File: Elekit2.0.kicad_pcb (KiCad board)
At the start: 2 copper layers, 25 parts, among them J1 USB_C_Receptacle_USB2.0, Q1 AO3401A, SW1 SW_Push, SW2 SW_Push, U1 ESP32-C3-WROOM-02-H4, U2 XC6206P332MR, U3 SRV05-4-P-T7

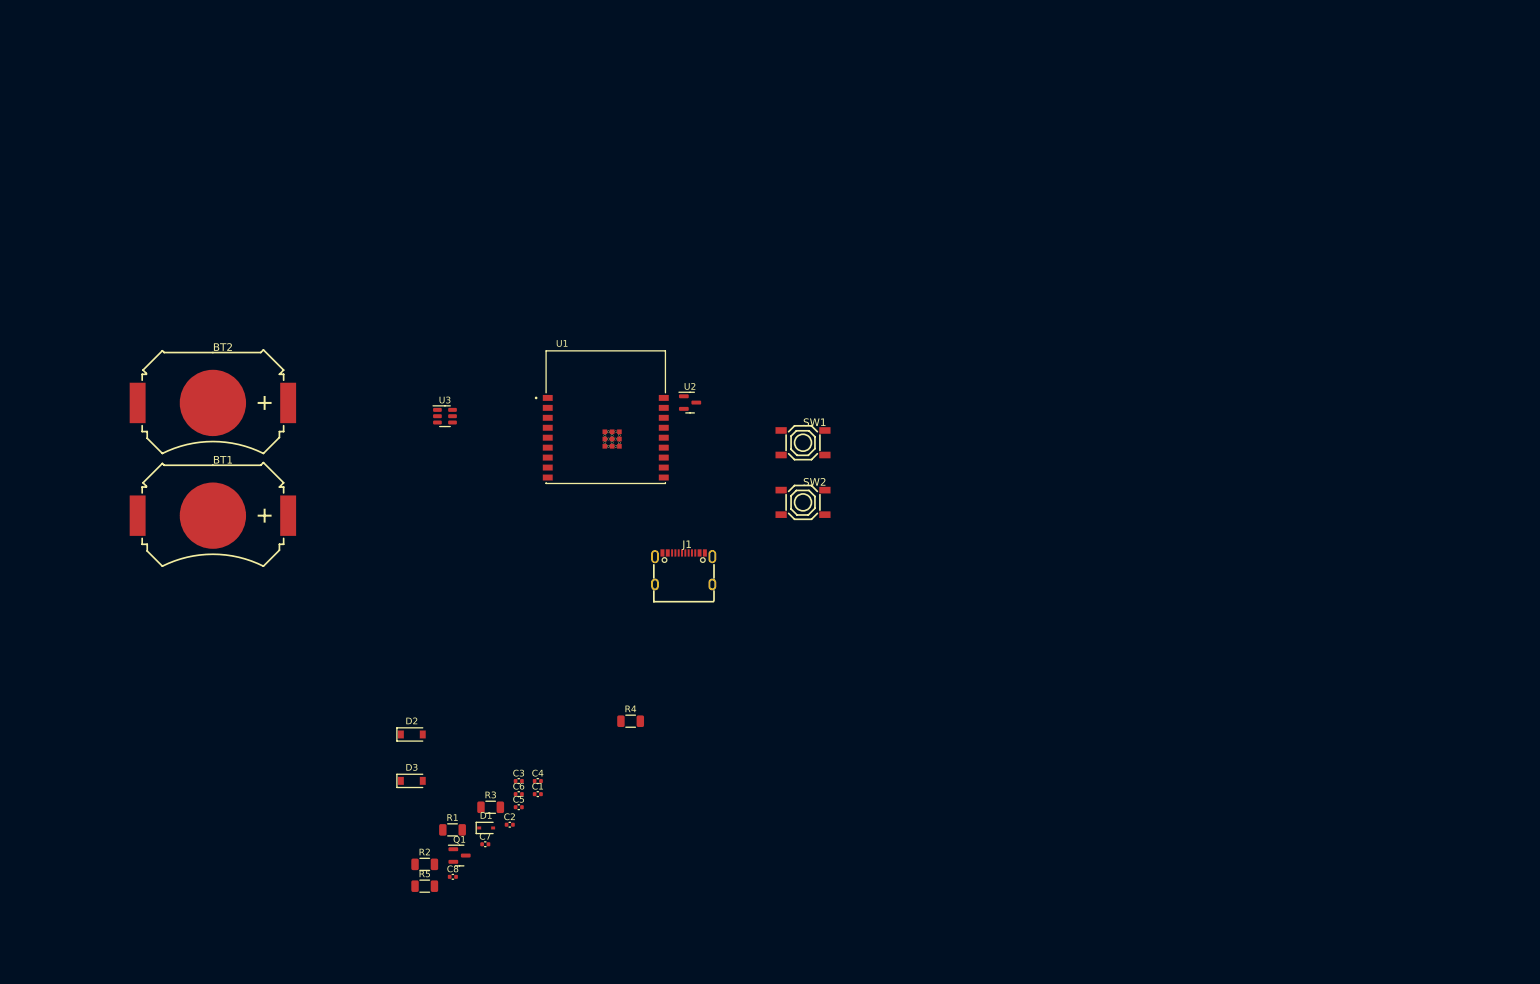
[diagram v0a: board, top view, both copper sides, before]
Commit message: Add libraries for used JLCPCB parts. Replace used parts with JLCPCB parts. Start adding LCD support using a shift register
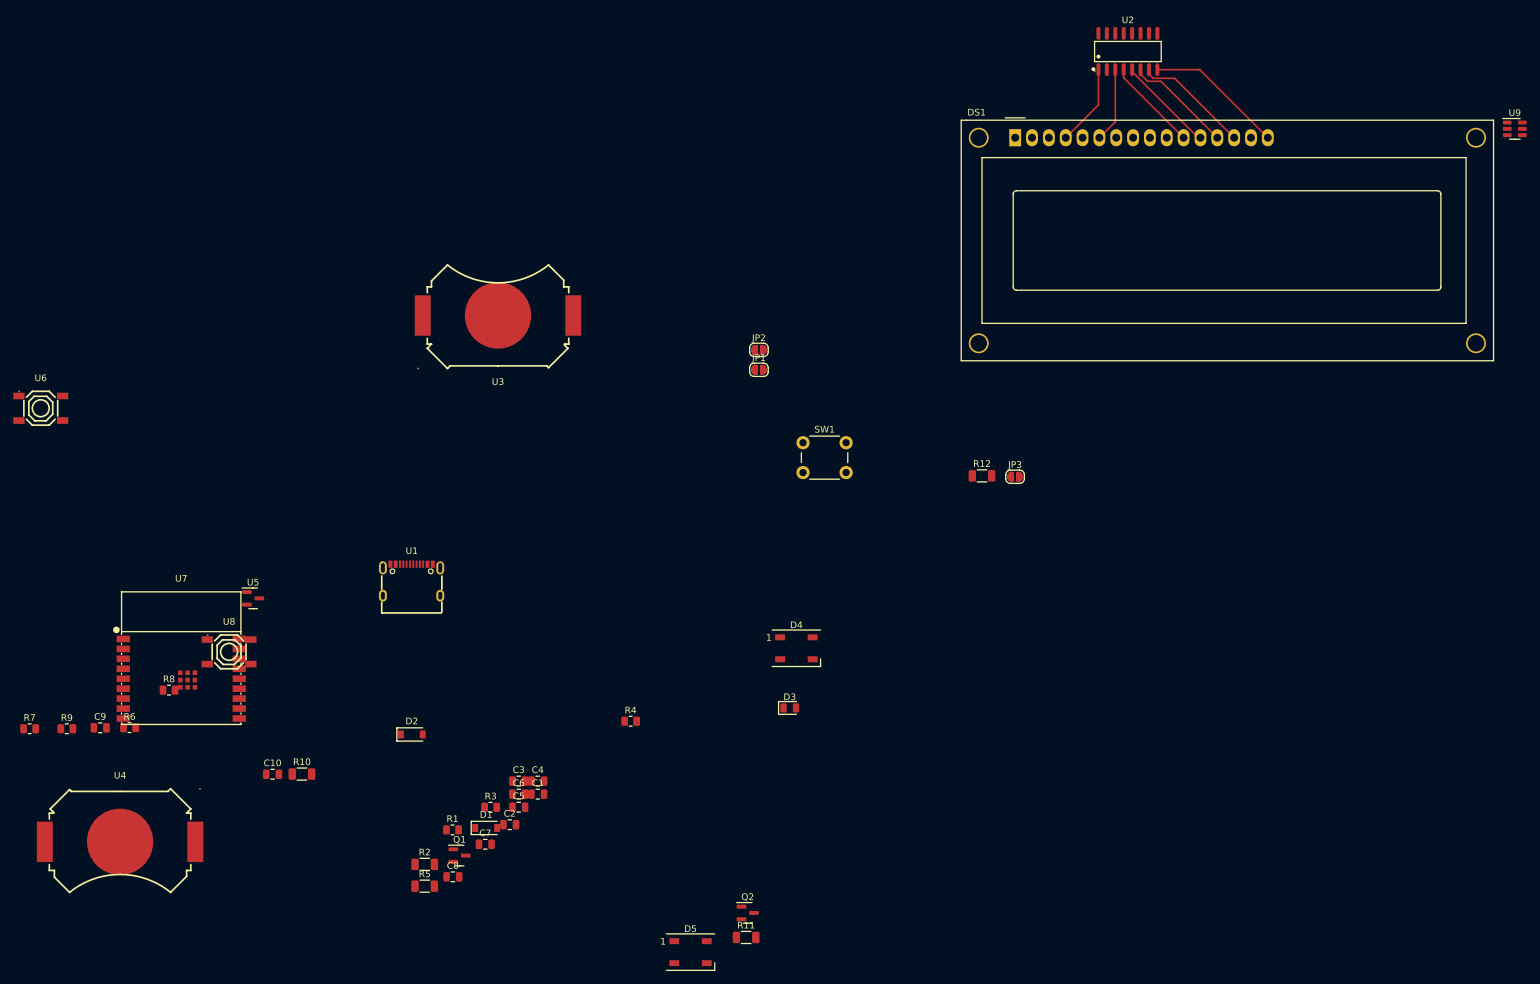
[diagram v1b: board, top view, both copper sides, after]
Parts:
- removed BT1, BT2: Battery_Cell, Footprint Libaries:BAT-SMD_MY-2032-12
- removed J1: USB_C_Receptacle_USB2.0, Footprint Libaries:USB-C-SMD_TYPE-C-6PIN-2MD-073
- removed SW2: SW_Push, Footprint Libaries:SW-SMD_4P-L5.1-W5.1-P3.70-LS6.5-TL-2
- added C10: 0.1u, Capacitor_SMD:C_0805_2012Metric, F.Cu at (87.0, 134.0)
- added C9: 0.1u, Capacitor_SMD:C_0805_2012Metric, F.Cu at (61.0, 127.0)
- added D4: WS2812B, LED_SMD:LED_WS2812B_PLCC4_5.0x5.0mm_P3.2mm, F.Cu at (166.0, 115.0)
- added D5: WS2812B, LED_SMD:LED_WS2812B_PLCC4_5.0x5.0mm_P3.2mm, F.Cu at (150.0, 160.8)
- added DS1: WC1602A, Display:WC1602A, F.Cu at (199.0, 38.0)
- added JP1: SolderJumper_2_Open, Jumper:SolderJumper-2_P1.3mm_Open_RoundedPad1.0x1.5mm, F.Cu at (160.3, 73.0)
- added JP2: SolderJumper_2_Open, Jumper:SolderJumper-2_P1.3mm_Open_RoundedPad1.0x1.5mm, F.Cu at (160.3, 70.0)
- added JP3: SolderJumper_2_Open, Jumper:SolderJumper-2_P1.3mm_Open_RoundedPad1.0x1.5mm, F.Cu at (199.0, 89.1)
- added Q2: 2N7002, Package_TO_SOT_SMD:SOT-23, F.Cu at (158.7, 154.9)
- added R10: 10k, Resistor_SMD:R_1206_3216Metric, F.Cu at (91.4, 134.0)
- added R11: 10k, Resistor_SMD:R_1206_3216Metric, F.Cu at (158.4, 158.6)
- added R12: 10k, Resistor_SMD:R_1206_3216Metric, F.Cu at (194.0, 89.0)
- added R6: 1k, Resistor_SMD:R_0805_2012Metric, F.Cu at (65.4, 127.0)
- added R7: 1k, Resistor_SMD:R_0805_2012Metric, F.Cu at (50.4, 127.1)
- added R8: 1k, Resistor_SMD:R_0805_2012Metric, F.Cu at (71.4, 121.3)
- added R9: 5.1k, Resistor_SMD:R_0805_2012Metric, F.Cu at (56.0, 127.1)
- added U4: MY-2032-12, 0_JLCPCB_Footprints:BAT-SMD_MY-2032-12, F.Cu at (64.0, 144.0)
- added U5: XC6206P332MR, Package_TO_SOT_SMD:SOT-23, F.Cu at (84.1, 107.5)
- added U6: TS-1187A-B-A-B, 0_JLCPCB_Footprints:SW-SMD_4P-L5.1-W5.1-P3.70-LS6.5-TL-2, F.Cu at (52.0, 78.8)
- added U7: ESP32-C3-WROOM-02-N4(4MB), 0_JLCPCB_Footprints:BULETM-SMD_ESPRESSIF_ESP32-C3-WROOM-02-N4-4MB, F.Cu at (73.2, 116.5)
- added U8: TS-1187A-B-A-B, 0_JLCPCB_Footprints:SW-SMD_4P-L5.1-W5.1-P3.70-LS6.5-TL-2, F.Cu at (80.4, 115.5)
- added U9: SRV05-4-P-T7, Package_TO_SOT_SMD:SOT-23-6, F.Cu at (274.4, 36.7)
- C1, C2: value 1u -> 0.1u; footprint Capacitor_SMD:C_0402_1005Metric -> Capacitor_SMD:C_0805_2012Metric
- C3: value 0.1u -> 4.7n; footprint Capacitor_SMD:C_0402_1005Metric -> Capacitor_SMD:C_0805_2012Metric
- C4, C6: value 0.1u -> 1u; footprint Capacitor_SMD:C_0402_1005Metric -> Capacitor_SMD:C_0805_2012Metric
- C5: value 10u -> 1u; footprint Capacitor_SMD:C_0402_1005Metric -> Capacitor_SMD:C_0805_2012Metric
- C7: footprint Capacitor_SMD:C_0402_1005Metric -> Capacitor_SMD:C_0805_2012Metric
- C8: value 0.1u -> 10u; footprint Capacitor_SMD:C_0402_1005Metric -> Capacitor_SMD:C_0805_2012Metric
- D1: value 1N5819WS -> B5819W; footprint Diode_SMD:D_SOD-323 -> Diode_SMD:D_SOD-123
- D3: value B5819W -> LED; footprint Diode_SMD:D_SOD-123 -> LED_SMD:LED_0805_2012Metric
- R1: footprint Resistor_SMD:R_1206_3216Metric -> Resistor_SMD:R_0805_2012Metric
- R2: value 5.1k -> 1M
- R3: value 10k -> 1k; footprint Resistor_SMD:R_1206_3216Metric -> Resistor_SMD:R_0805_2012Metric
- R4: value 10k -> 5.1k; footprint Resistor_SMD:R_1206_3216Metric -> Resistor_SMD:R_0805_2012Metric
- SW1: footprint Footprint Libaries:SW-SMD_4P-L5.1-W5.1-P3.70-LS6.5-TL-2 -> Button_Switch_THT:SW_PUSH_6mm
- U1: value ESP32-C3-WROOM-02-H4 -> TYPE-C_16PIN_2MD(073); footprint ELEKIT 2:MODULE_ESP32-C3-WROOM-02-H4 -> 0_JLCPCB_Footprints:USB-C-SMD_TYPE-C-6PIN-2MD-073
- U2: value XC6206P332MR -> 74HC595; footprint Package_TO_SOT_SMD:SOT-23 -> 0_JLCPCB_Footprints:SOIC-16_L9.9-W3.9-P1.27-LS6.0-BL
- U3: value SRV05-4-P-T7 -> MY-2032-12; footprint Package_TO_SOT_SMD:SOT-23-6 -> 0_JLCPCB_Footprints:BAT-SMD_MY-2032-12
- moved U2 84.6 mm to (216.0, 25.0)
- moved D3 58.1 mm to (165.0, 124.0)
- moved U1 39.0 mm to (108.0, 106.0)
- moved U3 17.0 mm to (121.0, 65.0), turned to 180 degrees
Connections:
- C1 pad 1: /VBUS -> GND
- C1 pad 2: GND -> /D+
- C2 pad 1: +3.3V -> GND
- C2 pad 2: GND -> /D-
- C3 pad 1: GND -> Net-(C3-Pad1)
- C3 pad 2: /D- -> GND
- C4 pad 1: GND -> Net-(C4-Pad1)
- C4 pad 2: /D+ -> GND
- C5 pad 1: +3.3V -> Net-(C5-Pad1)
- C8 pad 1: /CHIP_PU -> +3.3V
- D1 pad 1: unconnected-(D1-Pad1) -> /VBUS
- D1 pad 2: unconnected-(D1-Pad2) -> +BATT
- D2 pad 2: +BATT -> /VUSB
- D3 pad 1: /VBUS -> GND
- D3 pad 2: /VUSB -> Net-(D3-Pad2)
- Q1 pad 1: unconnected-(Q1-Pad1) -> Net-(C5-Pad1)
- Q1 pad 2: unconnected-(Q1-Pad2) -> /VBUS
- Q1 pad 3: unconnected-(Q1-Pad3) -> Net-(C4-Pad1)
- R1 pad 1: Net-(J1-PadA5) -> GND
- R1 pad 2: GND -> Net-(R1-Pad2)
- R2 pad 1: Net-(J1-PadB5) -> Net-(C3-Pad1)
- R3 pad 1: /CHIP_PU -> Net-(R3-Pad1)
- R4 pad 1: Net-(U1-Pad7) -> GND
- R4 pad 2: +3.3V -> Net-(R4-Pad2)
- R5 pad 1: Net-(D4-Pad2) -> Net-(C5-Pad1)
- R5 pad 2: +3.3V -> /VBUS
- SW1 pad 1: /GPIO9 -> GND
- SW1 pad 2: unconnected-(SW1-Pad2) -> Net-(R6-Pad2)
- U1 pad 1: +3.3V -> GND
- U1 pad 10: unconnected-(U1-Pad10) -> Net-(R4-Pad2)
- U1 pad 11: unconnected-(U1-Pad11) -> /VUSB
- U1 pad 12: unconnected-(U1-Pad12) -> GND
- U1 pad 13: /D- -> Net-(C3-Pad1)
- U1 pad 14: /D+ -> Net-(C3-Pad1)
- U1 pad 2: /CHIP_PU -> /VUSB
- U1 pad 4: unconnected-(U1-Pad4) -> Net-(R1-Pad2)
- U1 pad 5: unconnected-(U1-Pad5) -> /D-
- U1 pad 6: unconnected-(U1-Pad6) -> /D+
- U1 pad 7: Net-(U1-Pad7) -> /D-
- U1 pad 8: unconnected-(U1-Pad8) -> /D+
- U1 pad 9: GND -> unconnected-(U1-Pad9)
- U2 pad 1: GND -> Net-(U2-Pad1)
- U2 pad 2: +3.3V -> unconnected-(U2-Pad2)
- U2 pad 3: /VBUS -> Net-(U2-Pad3)
- U3 pad 1: /D+ -> +BATT
- U3 pad 2: GND -> Net-(U3-Pad2)
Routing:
- net GND: track 0.00 -> 20.9 mm
- net Net-(U2-Pad7): track 0.00 -> 17.5 mm
- net Net-(U2-Pad6): track 0.00 -> 16.2 mm
- net Net-(U2-Pad5): track 0.00 -> 14.7 mm
- net Net-(DS1-Pad11): track 0.00 -> 14.0 mm
- net Net-(U2-Pad1): track 0.00 -> 12.3 mm
- net Net-(U2-Pad3): track 0.00 -> 11.3 mm

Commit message: Update libraries. Finish LCD connector. save before changing LDO
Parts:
- added C11: 10u, Capacitor_SMD:C_0805_2012Metric, F.Cu at (37.3, 55.7)
- added C12: 0.1u, Capacitor_SMD:C_0805_2012Metric, F.Cu at (66.1, 73.0)
- added H1: MountingHole_Pad, MountingHole:MountingHole_3.2mm_M3_Pad_Via, F.Cu at (114.5, 72.5)
- added H2: MountingHole_Pad, MountingHole:MountingHole_3.2mm_M3_Pad_Via, F.Cu at (115.0, 25.0)
- added H3: MountingHole_Pad, MountingHole:MountingHole_3.2mm_M3_Pad_Via, F.Cu at (25.0, 25.0)
- added H4: MountingHole_Pad, MountingHole:MountingHole_3.2mm_M3_Pad_Via, F.Cu at (25.5, 71.5)
- added Q3: S8050, Package_TO_SOT_THT:TO-92_Inline, F.Cu at (84.7, 71.0)
- added Q4: 2N7002, Package_TO_SOT_SMD:SOT-23, F.Cu at (37.5, 52.0)
- added R13: 10k, Resistor_SMD:R_1206_3216Metric, F.Cu at (25.7, 57.8)
- added R14: 10k, Resistor_SMD:R_1206_3216Metric, F.Cu at (31.3, 57.8)
- added R15: 10k, Resistor_SMD:R_1206_3216Metric, F.Cu at (60.5, 73.0)
- added RV1: 10k, Potentiometer_THT:Potentiometer_Bourns_3296W_Vertical, B.Cu at (32.0, 75.0)
- C3: value 4.7n -> 0.1u
- C4: value 1u -> 4.7n
- C5: value 1u -> 0.1u
- C7: value 0.1u -> 1u
- C8: value 10u -> 1u
- D2: value B5819W -> LED; footprint Diode_SMD:D_SOD-123 -> LED_SMD:LED_0805_2012Metric
- D3: value LED -> B5819W; footprint LED_SMD:LED_0805_2012Metric -> Diode_SMD:D_SOD-123
- DS1: moved to B.Cu
- JP1: value SolderJumper_2_Open -> Power LED; moved to B.Cu
- JP2: value SolderJumper_2_Open -> Latch bypass; moved to B.Cu
- JP3: value SolderJumper_2_Open -> Power latch; moved to B.Cu
- Q1: value AO3401A -> S8050; footprint Package_TO_SOT_SMD:SOT-23 -> Package_TO_SOT_THT:TO-92_Inline
- Q2: value 2N7002 -> AO3401A
- R1, R9: value 5.1k -> 1k
- R10, R11: value 10k -> 1k; footprint Resistor_SMD:R_1206_3216Metric -> Resistor_SMD:R_0805_2012Metric
- R12, R5: value 10k -> 5.1k; footprint Resistor_SMD:R_1206_3216Metric -> Resistor_SMD:R_0805_2012Metric
- R2: value 1M -> 5.1k; footprint Resistor_SMD:R_1206_3216Metric -> Resistor_SMD:R_0805_2012Metric
- R3: value 1k -> 1M; footprint Resistor_SMD:R_0805_2012Metric -> Resistor_SMD:R_1206_3216Metric
- R4: value 5.1k -> 220R
- R6, R7, R8: value 1k -> 10k; footprint Resistor_SMD:R_0805_2012Metric -> Resistor_SMD:R_1206_3216Metric
- U1: value TYPE-C_16PIN_2MD(073) -> MY-2032-12; footprint 0_JLCPCB_Footprints:USB-C-SMD_TYPE-C-6PIN-2MD-073 -> 0_JLCPCB_Footprints:BAT-SMD_MY-2032-12
- U2: value 74HC595 -> TYPE-C_16PIN_2MD(073); footprint 0_JLCPCB_Footprints:SOIC-16_L9.9-W3.9-P1.27-LS6.0-BL -> 0_JLCPCB_Footprints:USB-C-SMD_TYPE-C-6PIN-2MD-073
- U4: value MY-2032-12 -> 74HC595; footprint 0_JLCPCB_Footprints:BAT-SMD_MY-2032-12 -> 0_JLCPCB_Footprints:SOIC-16_L9.9-W3.9-P1.27-LS6.0-BL
- U7: value ESP32-C3-WROOM-02-N4(4MB) -> TS-1187A-B-A-B; footprint 0_JLCPCB_Footprints:BULETM-SMD_ESPRESSIF_ESP32-C3-WROOM-02-N4-4MB -> 0_JLCPCB_Footprints:SW-SMD_4P-L5.1-W5.1-P3.70-LS6.5-TL-2
- U8: value TS-1187A-B-A-B -> ESP32-C3-WROOM-02-N4(4MB); footprint 0_JLCPCB_Footprints:SW-SMD_4P-L5.1-W5.1-P3.70-LS6.5-TL-2 -> 0_JLCPCB_Footprints:BULETM-SMD_ESPRESSIF_ESP32-C3-WROOM-02-N4-4MB
- moved U9 238.0 mm to (36.5, 45.0)
- moved U2 194.2 mm to (23.0, 47.0), turned to -90 degrees
- moved R11 164.6 mm to (30.9, 54.6)
- moved DS1 160.9 mm to (39.9, 62.0)
- moved D3 153.3 mm to (30.5, 50.5)
- moved Q2 142.4 mm to (68.7, 44.5)
- moved JP3 128.3 mm to (74.5, 58.0), turned to 180 degrees
- moved R12 123.9 mm to (71.1, 73.0)
- moved R4 123.9 mm to (37.3, 58.2)
- moved C4 117.8 mm to (46.0, 49.5)
- moved C1 117.8 mm to (46.0, 51.5)
- moved C3 117.8 mm to (43.1, 49.5)
- moved C5 117.8 mm to (43.1, 53.5)
- moved C6 117.8 mm to (43.1, 51.5)
- moved C8 113.1 mm to (78.0, 42.4)
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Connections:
- C1 pad 1: GND -> /VBUS
- C1 pad 2: /D+ -> GND
- C2 pad 2: /D- -> /D+
- C3 pad 1: Net-(C3-Pad1) -> GND
- C3 pad 2: GND -> /D-
- C5 pad 1: Net-(C5-Pad1) -> /VBUS
- C6 pad 1: +3.3V -> Net-(C6-Pad1)
- C7 pad 1: /GPIO9 -> Net-(C7-Pad1)
- C9 pad 1: +3.3V -> /GPIO9
- D2 pad 1: /VBUS -> GND
- D2 pad 2: /VUSB -> Net-(D2-Pad2)
- D3 pad 1: GND -> /VBUS
- D3 pad 2: Net-(D3-Pad2) -> /VUSB
- DS1 pad 12: Net-(U2-Pad5) -> Net-(DS1-Pad12)
- DS1 pad 13: Net-(U2-Pad6) -> Net-(DS1-Pad13)
- DS1 pad 14: Net-(U2-Pad7) -> Net-(DS1-Pad14)
- DS1 pad 15: unconnected-(DS1-Pad15) -> Net-(DS1-Pad15)
- DS1 pad 2: unconnected-(DS1-Pad2) -> /VBUS
- DS1 pad 3: unconnected-(DS1-Pad3) -> Net-(DS1-Pad3)
- DS1 pad 4: Net-(U2-Pad1) -> Net-(DS1-Pad4)
- DS1 pad 6: Net-(U2-Pad3) -> Net-(DS1-Pad6)
- JP1 pad 1: Net-(D3-Pad2) -> Net-(D2-Pad2)
- JP1 pad 2: Net-(R3-Pad1) -> Net-(JP1-Pad2)
- JP2 pad 1: Net-(C4-Pad1) -> Net-(C6-Pad1)
- Q1 pad 1: Net-(C5-Pad1) -> /RTS
- Q1 pad 2: /VBUS -> Net-(Q1-Pad2)
- Q1 pad 3: Net-(C4-Pad1) -> /CHIP_PU
- Q2 pad 1: Net-(Q2-Pad1) -> Net-(C7-Pad1)
- Q2 pad 2: GND -> /VBUS
- Q2 pad 3: Net-(D4-Pad4) -> Net-(C6-Pad1)
- R1 pad 1: GND -> Net-(JP1-Pad2)
- R1 pad 2: Net-(R1-Pad2) -> +3.3V
- R10 pad 1: /CHIP_PU -> Net-(C7-Pad1)
- R10 pad 2: +3.3V -> Net-(JP3-Pad2)
- R11 pad 1: Net-(R11-Pad1) -> Net-(Q4-Pad1)
- R11 pad 2: +3.3V -> /GPIO5
- R12 pad 1: Net-(R12-Pad1) -> /VBUS
- R12 pad 2: +3.3V -> Net-(D4-Pad4)
- R2 pad 1: Net-(C3-Pad1) -> GND
- R2 pad 2: GND -> Net-(R2-Pad2)
- R3 pad 1: Net-(R3-Pad1) -> Net-(C4-Pad1)
- R3 pad 2: +3.3V -> GND
- R4 pad 1: GND -> /VBUS
- R4 pad 2: Net-(R4-Pad2) -> Net-(DS1-Pad15)
- R5 pad 1: Net-(C5-Pad1) -> GND
- R5 pad 2: /VBUS -> Net-(R5-Pad2)
- R6 pad 1: Net-(C5-Pad1) -> Net-(Q1-Pad2)
- R6 pad 2: Net-(R6-Pad2) -> /DTR
- R7 pad 1: Net-(C5-Pad1) -> Net-(C7-Pad1)
- R7 pad 2: Net-(JP3-Pad2) -> /VBUS
- R8 pad 1: Net-(Q2-Pad1) -> Net-(Q3-Pad2)
- R8 pad 2: /GPIO5 -> /RTS
- R9 pad 1: /VBUS -> Net-(C7-Pad1)
- R9 pad 2: Net-(D4-Pad4) -> Net-(R9-Pad2)
- SW1 pad 2: Net-(R6-Pad2) -> Net-(R9-Pad2)
- U1 pad 1: GND -> +BATT
- U1 pad 2: /VUSB -> Net-(U1-Pad2)
- U2 pad 1: Net-(U2-Pad1) -> GND
- U2 pad 10: unconnected-(U2-Pad10) -> Net-(R5-Pad2)
- U2 pad 11: unconnected-(U2-Pad11) -> /VUSB
- U2 pad 12: unconnected-(U2-Pad12) -> GND
- U2 pad 13: unconnected-(U2-Pad13) -> Net-(C4-Pad1)
- U2 pad 14: unconnected-(U2-Pad14) -> Net-(C4-Pad1)
- U2 pad 2: unconnected-(U2-Pad2) -> /VUSB
- U2 pad 3: Net-(U2-Pad3) -> unconnected-(U2-Pad3)
- U2 pad 4: Net-(DS1-Pad11) -> Net-(R2-Pad2)
- U2 pad 5: Net-(U2-Pad5) -> /D-
- U2 pad 6: Net-(U2-Pad6) -> /D+
- U2 pad 7: Net-(U2-Pad7) -> /D-
- U2 pad 8: GND -> /D+
- U3 pad 1: +BATT -> Net-(U1-Pad2)
- U3 pad 2: Net-(U3-Pad2) -> GND
- U4 pad 1: Net-(U3-Pad2) -> Net-(DS1-Pad4)
- U4 pad 2: GND -> unconnected-(U4-Pad2)
- U5 pad 3: Net-(C4-Pad1) -> Net-(C6-Pad1)
- U7 pad 1: +3.3V -> /CHIP_PU
- U7 pad 2: /CHIP_PU -> unconnected-(U7-Pad2)
- U7 pad 3: /GPIO4 -> unconnected-(U7-Pad3)
- U7 pad 4: /GPIO5 -> GND
- U8 pad 1: /CHIP_PU -> +3.3V
- U8 pad 2: unconnected-(U8-Pad2) -> /CHIP_PU
- U8 pad 3: unconnected-(U8-Pad3) -> /GPIO4
- U8 pad 4: GND -> /GPIO5
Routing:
- net GND: track 20.9 -> 0.00 mm
- net Net-(U2-Pad7): track 17.5 -> 0.00 mm
- net Net-(U2-Pad6): track 16.2 -> 0.00 mm
- net Net-(U2-Pad5): track 14.7 -> 0.00 mm
- net Net-(DS1-Pad11): track 14.0 -> 0.00 mm
- net Net-(U2-Pad1): track 12.3 -> 0.00 mm
- net Net-(U2-Pad3): track 11.3 -> 0.00 mm
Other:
- board outline added: 100 x 58.5 mm
